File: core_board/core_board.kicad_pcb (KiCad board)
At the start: 2 copper layers, 27 x 60 mm, 37 parts, among them J1 Conn_01x13_Socket, J2 Conn_01x13_Socket, J3 Ignitor Output, J4 Micro_SD_Card, J5 Battery Input, J7 Connector 1, J8 Connector 2, U1 CPC1002N, U2 CPC1002N, U3 CPC1002N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

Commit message: Fixed small potential issues
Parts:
- moved G*** 0.25 mm to (111.0, 103.0)
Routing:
- net GND: track 21.5 -> 17.0 mm, vias 21 -> 15
- net +3.3V: track 123.1 -> 125.2 mm
- net /SCL: track 25.7 -> 27.4 mm
- net Net-(U5-XIN32): track 9.53 -> 10.4 mm
- net /Ignitor Logic 3 +: track 35.2 -> 35.8 mm
- net Net-(D2-A): track 3.09 -> 2.55 mm

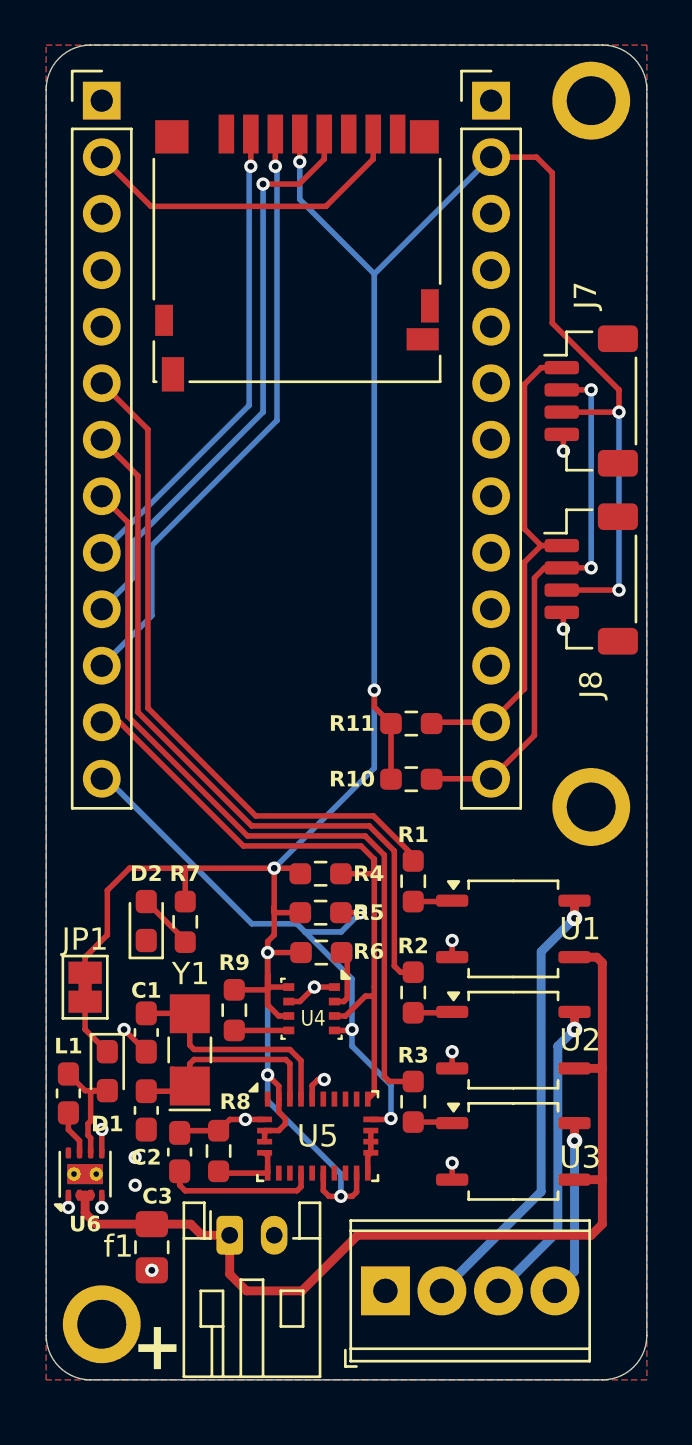
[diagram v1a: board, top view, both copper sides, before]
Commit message: Tweaked mounting holes, removed warning on back
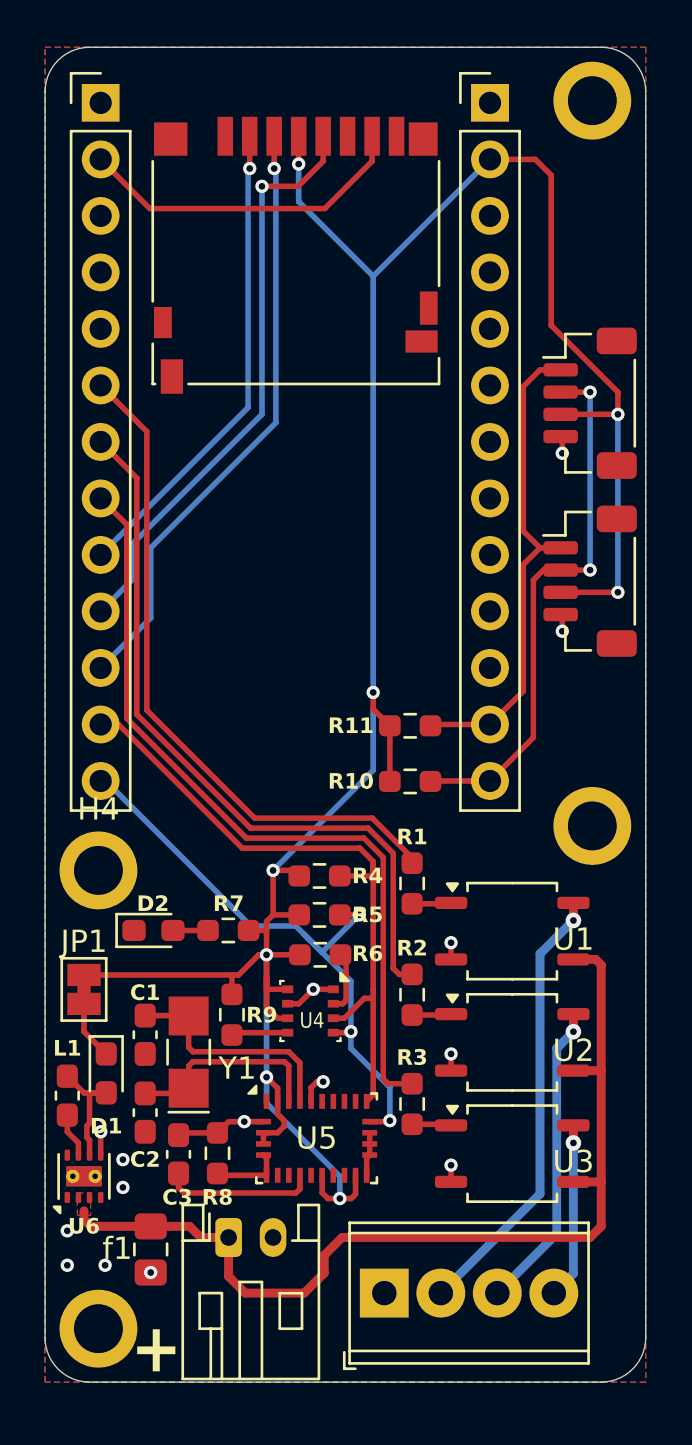
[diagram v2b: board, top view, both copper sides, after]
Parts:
- added H4: MountingHole, MountingHole:MountingHole_2.2mm_M2_ISO7380_Pad, F.Cu at (96.6, 95.6)
- moved R7 1.98 mm to (102.4, 98.3), turned to 0 degrees
- moved H2 0.85 mm to (118.8, 93.6)
- moved D2 0.54 mm to (99.1, 98.3), turned to 0 degrees
- moved H1 0.25 mm to (96.6, 116.2)
- moved R9 0.23 mm to (102.6, 102.1)
- moved J4 0.11 mm to (105.5, 68.0)
- moved U4 0.11 mm to (106.1, 101.9)
- moved JP1 0.11 mm to (96.0, 101.0)
- moved f1 0.11 mm to (99.0, 112.6)
- moved J1 0.11 mm to (114.2, 61.1)
- moved J2 0.11 mm to (96.7, 61.1)
- moved R4 0.11 mm to (106.5, 95.8)
- moved R5 0.11 mm to (106.5, 97.6)
- moved R6 0.11 mm to (106.6, 99.4)
- moved C1 0.11 mm to (98.7, 103.0)
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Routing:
- net +3.3V: track 125.2 -> 119.7 mm
- net GND: track 17.0 -> 14.5 mm
- net Net-(D2-A): track 2.55 -> 1.58 mm
- net /SCL: track 27.4 -> 28.1 mm
- net +BATT: track 43.9 -> 43.4 mm
- added copper zone on F.Cu, net +BATT
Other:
- board text added: "Specs: • 3 flight events • 3-16v battery input • Data logging • Altitude • Pressure • Temperature • Spatial orientation • Stemma QT expansion"
- board text removed: "Specs: • 3 flight events • 3-16v input • Data logging • Altitude • Pressure • Temperature • 9DoF Spatial orientation"
- board text removed: "WARNING: Do NOT power with USB and battery simultaneously It WILL break"

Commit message: Added open hardware logo
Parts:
- added G***: LOGO, LOGO, B.Cu at (107.2, 102.2)
- moved G*** 16.3 mm to (106.8, 87.2)
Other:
- board text added: "Rev 0.1.1"
- board text removed: "Rev 0.1.0"

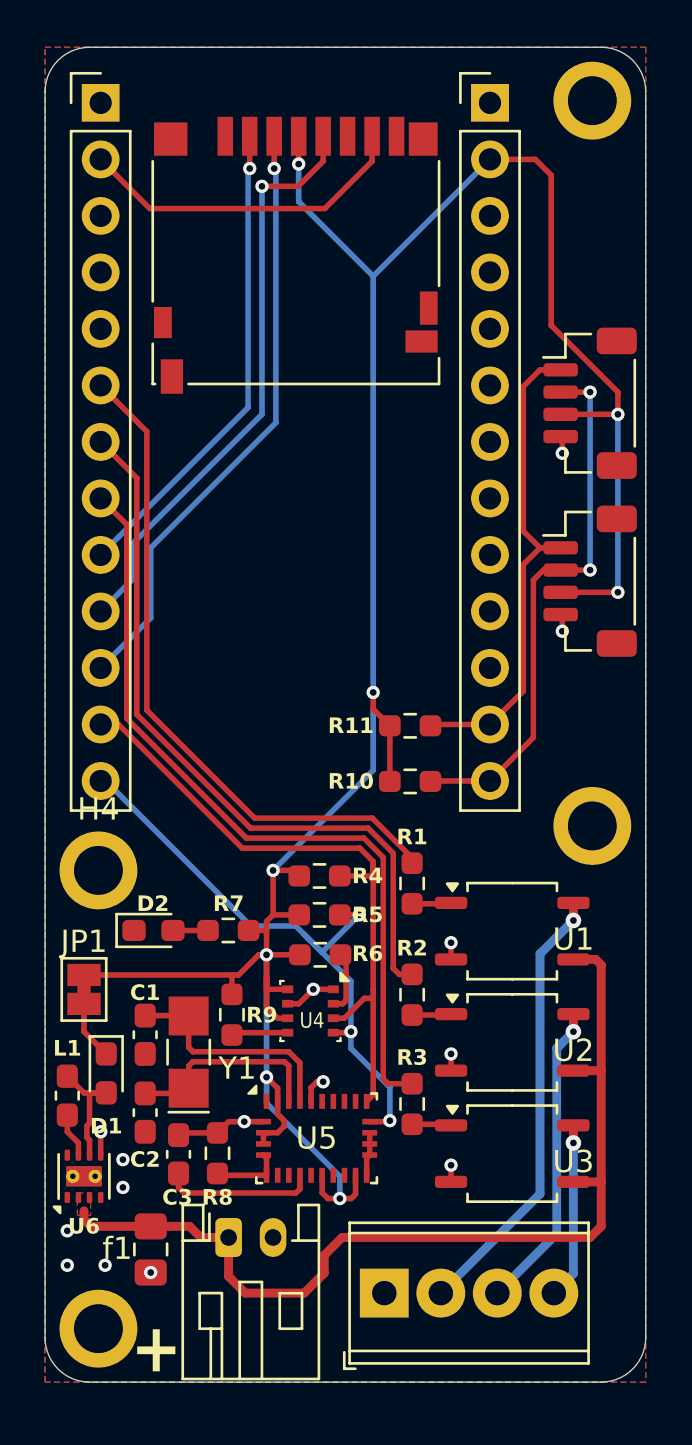
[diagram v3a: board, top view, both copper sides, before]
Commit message: Improved PCB layout some more
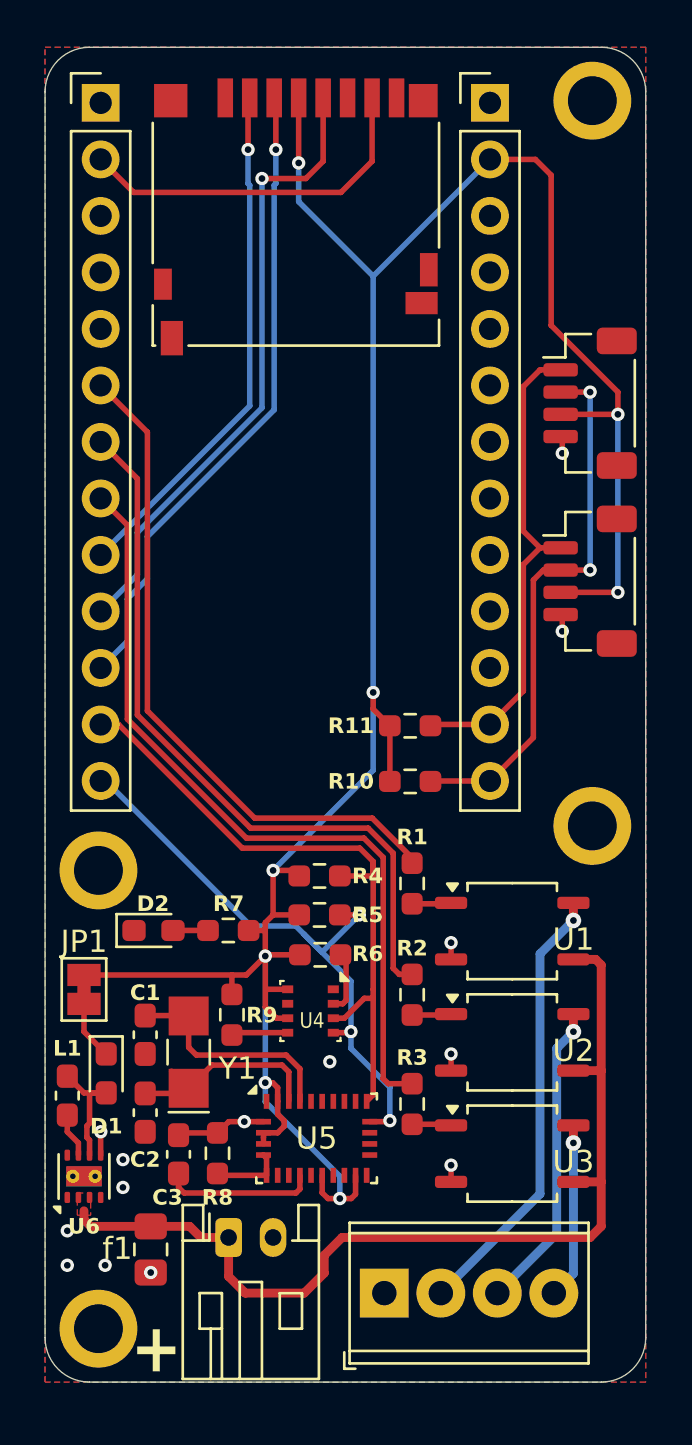
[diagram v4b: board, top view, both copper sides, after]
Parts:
- moved J4 1.73 mm to (105.5, 66.2)
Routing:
- net GND: track 14.5 -> 8.94 mm, vias 15 -> 14
- net /SPI SCK: track 26.5 -> 28.4 mm
- net /SPI CS: track 21.6 -> 23.4 mm
- net /SPI SDO: track 27.2 -> 28.9 mm
- net /SPI SDI: track 15.1 -> 16.2 mm
- net Net-(U5-XIN32): track 10.4 -> 9.52 mm
